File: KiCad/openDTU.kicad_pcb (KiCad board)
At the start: 4 copper layers, 40 x 50 mm, 48 parts, among them J1 USB_C_Receptacle_USB2.0, J2 Conn_Coaxial, J3 Micro_SD_Card, Q1 BC817, Q2 BC817, SW1 SW_Push, SW2 SW_Push, U1 CH340C, U3 ESP32-WROOM-32, U4 nRF24L01P, U5 NCP1117-3.3_SOT223, Y1 Crystal

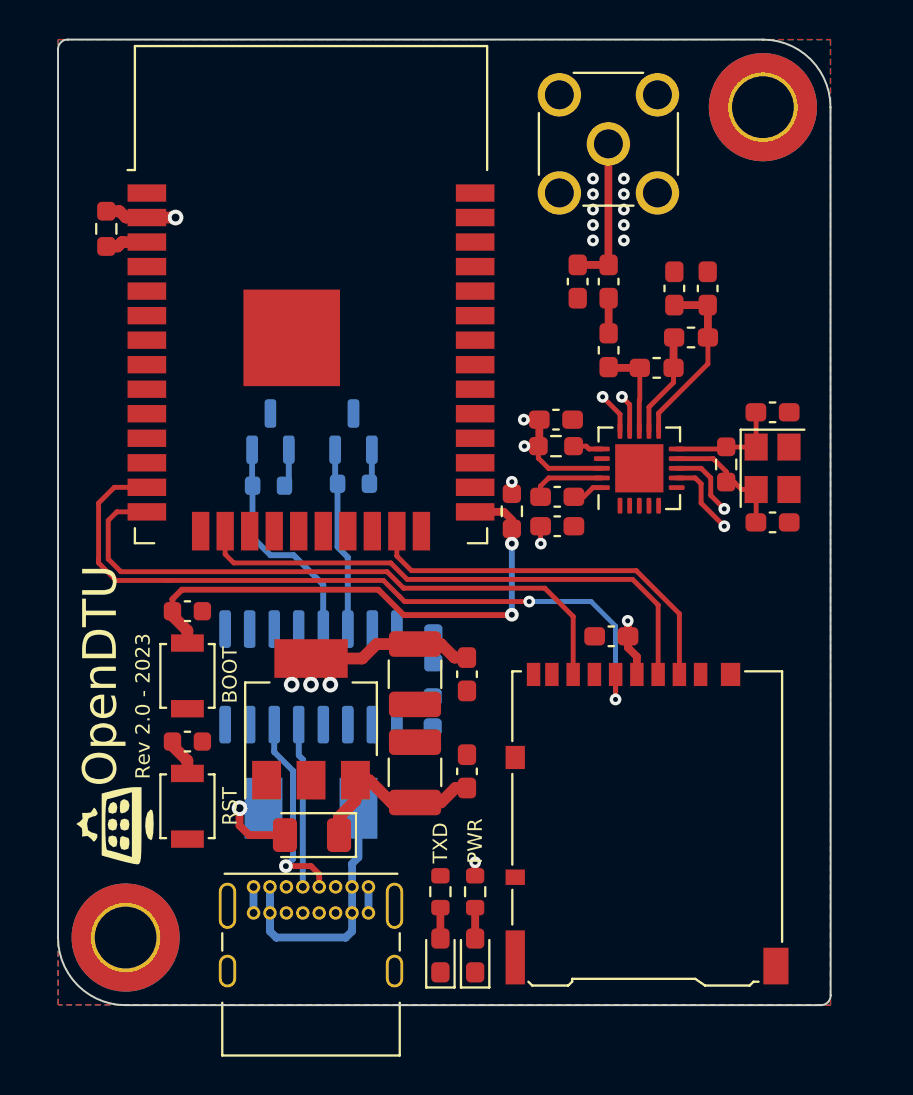
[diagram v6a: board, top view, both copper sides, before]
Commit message: adding pin header for I2C,SPI, etc.
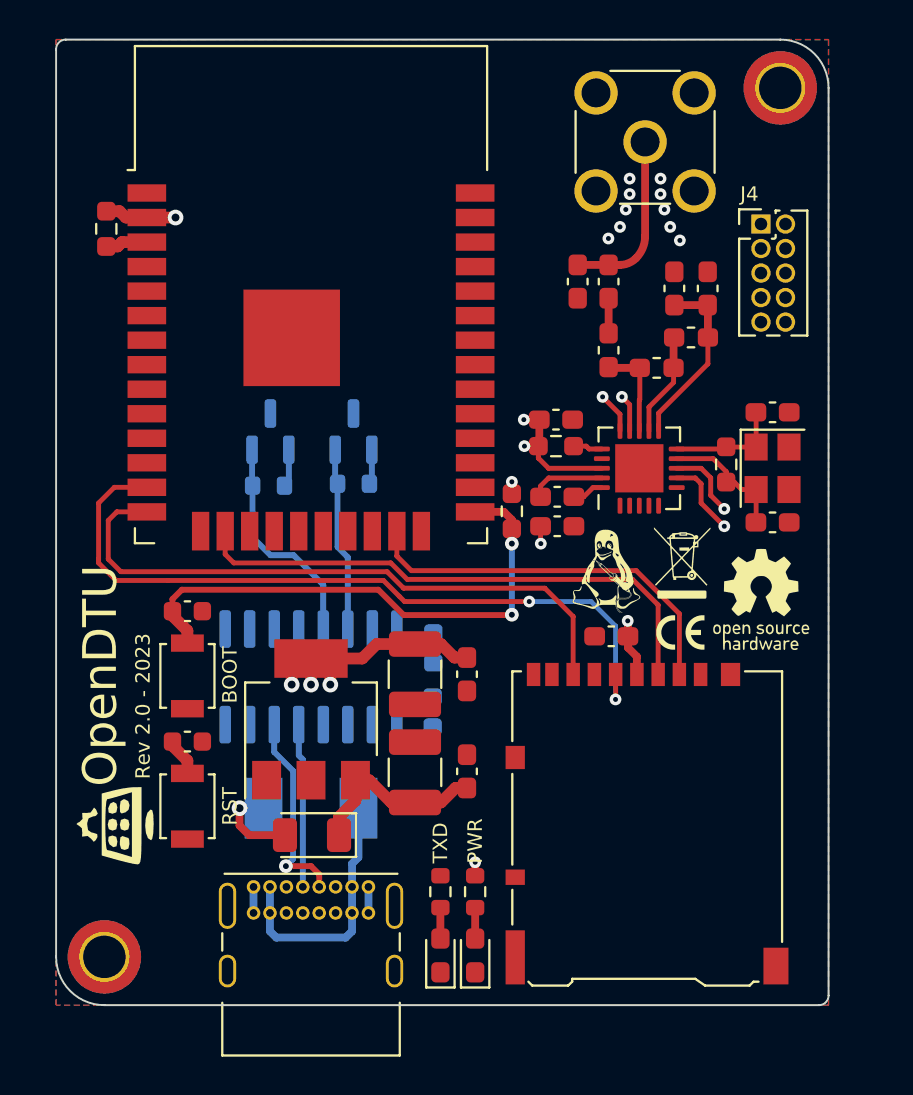
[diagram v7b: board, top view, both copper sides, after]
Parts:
- removed the REF** at (162.1, 71.5)
- removed the REF** at (129.1, 114.5)
- added G***: LOGO, LOGO, F.Cu at (154.0, 94.8)
- added G***: LOGO, LOGO, F.Cu at (157.8, 98.7)
- added G***: LOGO, LOGO, F.Cu at (158.0, 95.3)
- added G***: LOGO, LOGO, F.Cu at (162.0, 97.0)
- added J4: Conn_02x05_Counter_Clockwise, Connector_PinHeader_1.27mm:PinHeader_2x05_P1.27mm_Vertical, F.Cu at (162.0, 77.5)
- added REF**: MountingHole_2.2mm_M2_DIN965_Pad_TopBottom, MountingHole:MountingHole_2.2mm_M2_DIN965_Pad_TopBottom, F.Cu at (128.0, 115.5)
- added REF**: MountingHole_2.2mm_M2_DIN965_Pad_TopBottom, MountingHole:MountingHole_2.2mm_M2_DIN965_Pad_TopBottom, F.Cu at (163.0, 70.5)
- moved J2 1.90 mm to (156.0, 73.3)
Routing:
- net Net-(C10-Pad2): track 7.87 -> 9.26 mm
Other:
- outline, holes or cut-outs redrawn

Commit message: changing USB-C connector and switching GND and +3V3 inner layer
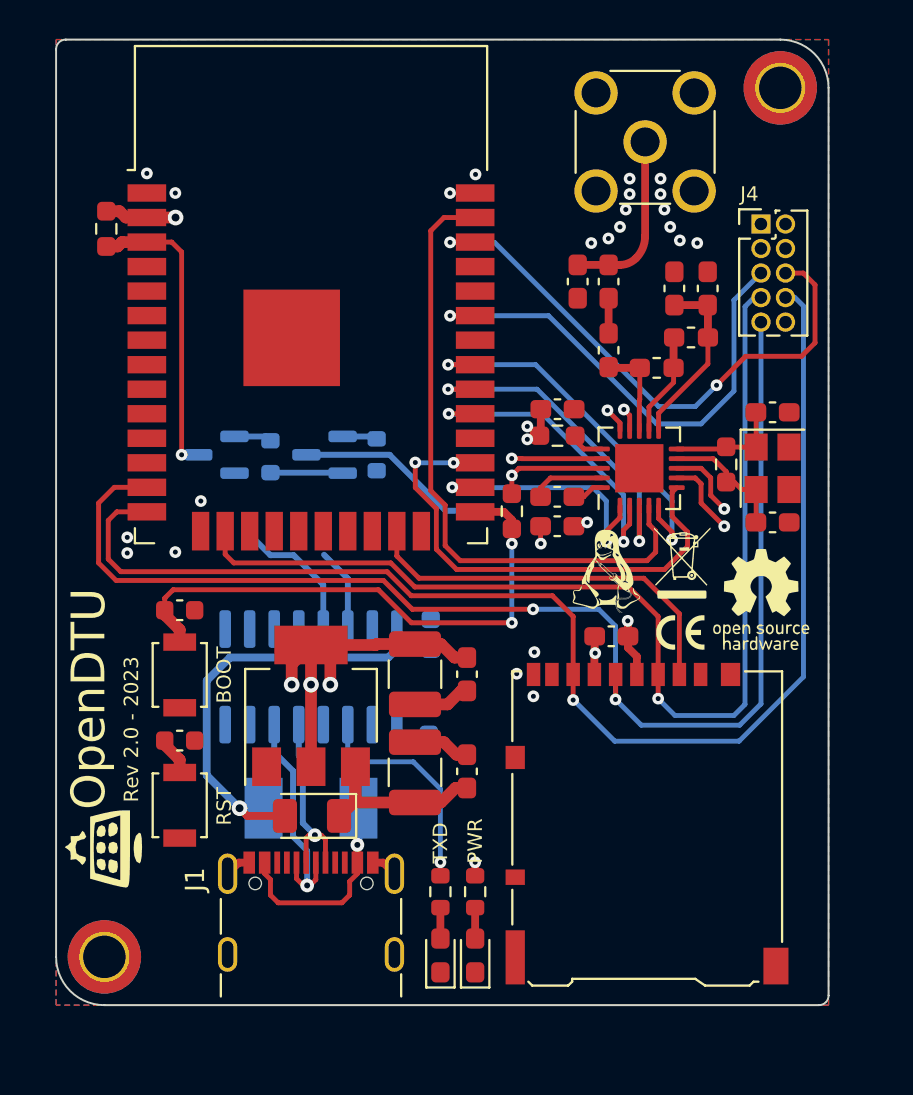
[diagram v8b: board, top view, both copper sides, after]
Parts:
- J1: footprint Connector_USB:USB_C_Receptacle_GCT_USB4085 -> Connector_USB:USB_C_Receptacle_GCT_USB4105-xx-A_16P_TopMnt_Horizontal
- moved J1 3.84 mm to (138.7, 114.3)
- moved Q1 3.05 mm to (133.8, 89.5), turned to 180 degrees
- moved Q2 1.92 mm to (139.4, 89.5), turned to 180 degrees
- moved R5 1.92 mm to (142.1, 89.5), turned to 90 degrees
- moved R4 1.50 mm to (136.6, 89.6), turned to 90 degrees
- moved G*** 1.34 mm to (127.9, 109.9)
- moved D1 0.99 mm to (138.8, 108.2)
- moved C16 0.71 mm to (144.9, 98.8), turned to 90 degrees
- moved U5 0.70 mm to (138.7, 102.5)
- moved C3 0.55 mm to (151.5, 87.1)
- moved R1 0.55 mm to (151.5, 88.5)
- moved C15 0.43 mm to (144.8, 103.2)
- moved C17 0.40 mm to (131.9, 97.5)
- moved C18 0.40 mm to (131.9, 104.3)
- moved SW1 0.40 mm to (131.9, 100.9)
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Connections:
- J1 pad B6: (no net) -> Net-(J1-PadA6)
- J1 pad B7: (no net) -> Net-(J1-PadA7)
- J4 pad 10: /ESP.SCL -> unconnected-(J4-Pad10)
- J4 pad 5: /ESP.MOSI -> /ESP.SDA
- J4 pad 6: /ESP.MISO -> /ESP.SCL
- J4 pad 7: /ESP.SCK -> /ESP.MOSI_SD
- J4 pad 8: unconnected-(J4-Pad8) -> /ESP.MISO_SD
- J4 pad 9: /ESP.SDA -> /ESP.SCK_SD
- R4 pad 1: Net-(Q1-Pad2) -> Net-(Q2-Pad2)
- R5 pad 1: Net-(Q2-Pad2) -> Net-(Q1-Pad2)
- REF** pad 1: (no net) -> GND (x2)
- U1 pad 13: Net-(Q1-Pad2) -> Net-(Q2-Pad2)
- U1 pad 14: Net-(Q2-Pad2) -> Net-(Q1-Pad2)
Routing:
- net /ESP.MISO_SD: track 32.5 -> 68.3 mm, vias 0 -> 1
- net /ESP.MOSI: track 0.00 -> 33.2 mm
- net /ESP.SCL: track 0.00 -> 29.9 mm, vias 0 -> 2
- net /ESP.SCK_SD: track 39.2 -> 67.5 mm
- net /ESP.MOSI_SD: track 28.3 -> 55.9 mm, vias 0 -> 1
- net /ESP.SDA: track 0.00 -> 25.7 mm, vias 0 -> 1
- net /ESP.IRQ: track 0.00 -> 25.5 mm, vias 0 -> 2
- net VBUS: track 4.70 -> 25.4 mm
- net /ESP.MISO: track 0.00 -> 20.0 mm, vias 0 -> 2
- net /ESP.SCK: track 0.00 -> 17.9 mm, vias 0 -> 2
- net /ESP.~{CS}: track 0.00 -> 16.6 mm, vias 0 -> 2
- net /ESP.CE: track 0.00 -> 13.7 mm, vias 0 -> 2
- net /ESP_EN: track 4.17 -> 17.5 mm, vias 0 -> 1
- net GND: track 10.1 -> 22.1 mm, vias 12 -> 28
- net /ESP.TXD: track 0.00 -> 11.6 mm, vias 0 -> 1
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- added copper zone on In2.Cu, net +3.3V
- added copper zone on In1.Cu, net GND
- removed copper zone on In1.Cu, net +3.3V
